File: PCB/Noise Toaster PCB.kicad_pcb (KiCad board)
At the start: 2 copper layers, 132.1 x 68.6 mm, 137 parts, among them J2 Power, J3 AREG, J4 LFO, J5 VCO, J6 VCO, J7 VCLPF, J8 VCA, J9 Amp, Q1 2N5457, Q10 2N3906, Q2 2N3904, Q3 2N3904, Q4 2N3904, Q5 2N3904, Q6 2N3904, Q7 2N5457, Q8 2N5457, Q9 2N5457, U1 LM324, U2 LM324, U3 LM386, X4 WNS

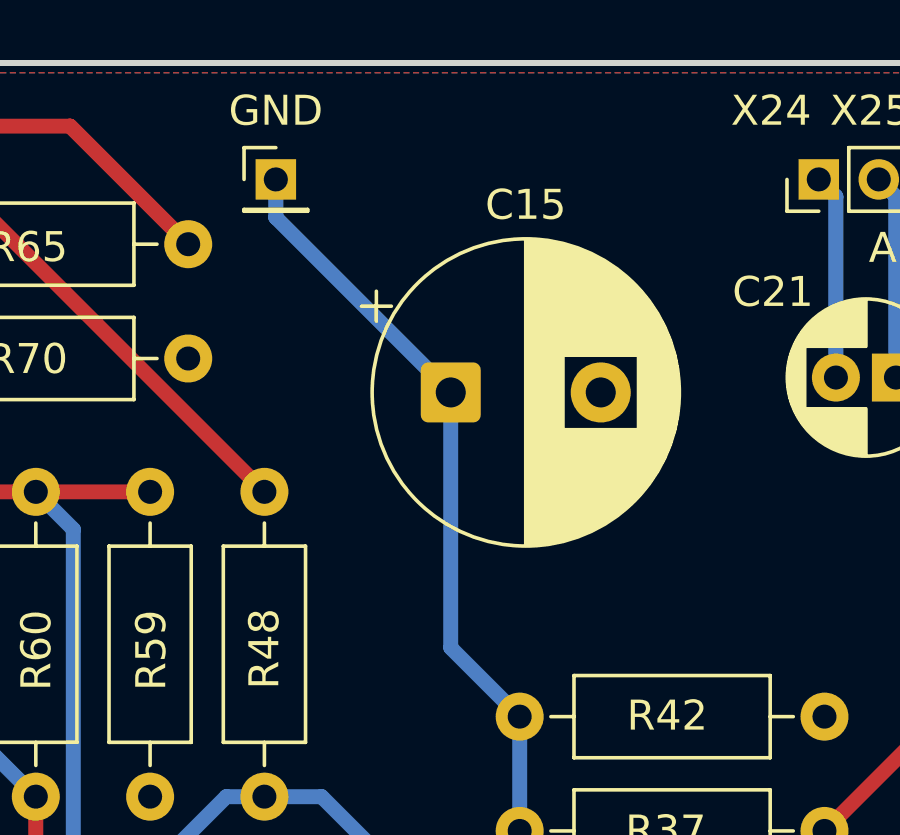
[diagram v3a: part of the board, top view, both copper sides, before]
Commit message: Added extra GND holes
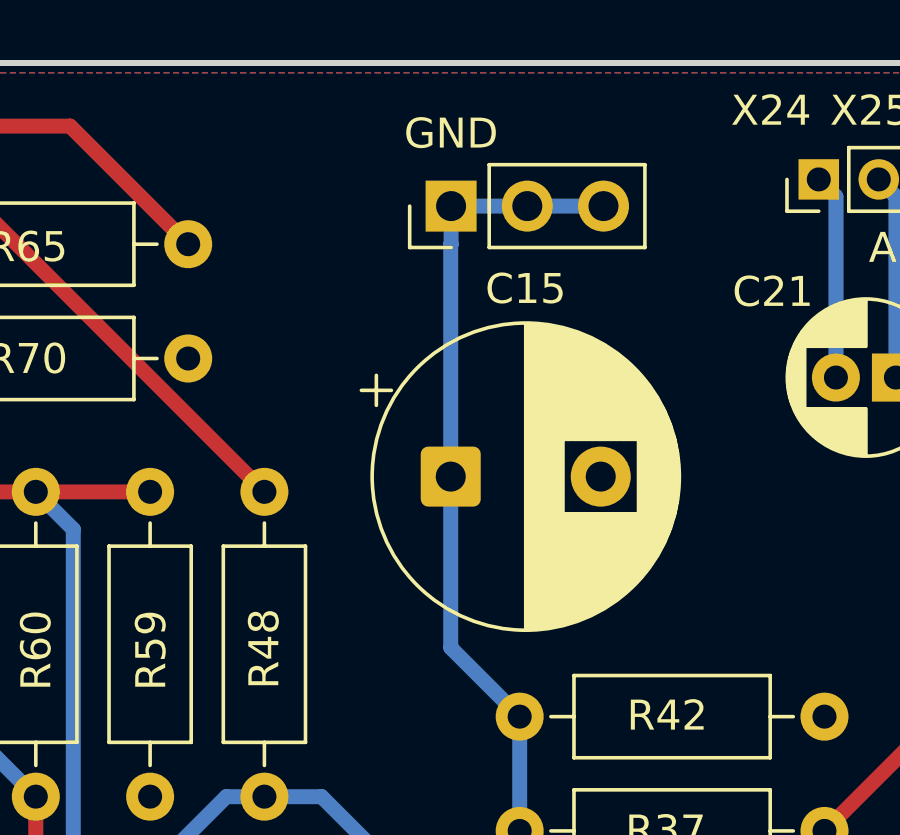
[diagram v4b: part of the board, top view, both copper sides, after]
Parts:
- GND: renamed from GND1; footprint Connector_PinHeader_2.00mm:PinHeader_1x01_P2.00mm_Vertical -> Connector_PinHeader_2.54mm:PinHeader_1x03_P2.54mm_Vertical
- moved GND 5.91 mm to (142.1, 80.0), turned to 90 degrees
- moved C15 2.81 mm to (142.1, 89.1)
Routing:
- net GND: track 160.9 -> 162.7 mm
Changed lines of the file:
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@@
 		)
 	)
-	(footprint "Connector_PinHeader_2.00mm:PinHeader_1x01_P2.00mm_Vertical"
+	(footprint "Connector_PinHeader_2.54mm:PinHeader_1x03_P2.54mm_Vertical"
 		(layer "F.Cu")
-		(at 136.302 79.148)
-		(descr "Through hole straight pin header, 1x01, 2.00mm pitch, single row")
-		(tags "Through hole pin header THT 1x01 2.00mm single row")
-		(property "Reference" "GND1"
-			(at 0 -2.06 0)
+		(at 142.144 80.037 90)
+		(descr "Through hole straight pin header, 1x03, 2.54mm pitch, single row")
+		(tags "Through hole pin header THT 1x03 2.54mm single row")
+		(property "Reference" "GND"
+			(at 2.413 0 180)
 			(layer "F.SilkS")
-			(hide yes)
 			(effects
 				(font
@@
 		)
 		(property "Value" "GND"
-			(at 0 -2.286 0)
-			(layer "F.SilkS")
+			(at 2.159 0 180)
+			(layer "F.Fab")
 			(effects
 				(font
@@
 		)
 		(property "Datasheet" ""
-			(at 0 0 0)
+			(at 0 0 90)
 			(layer "F.Fab")
 			(hide yes)
@@
 			)
 		)
-		(property "Description" "Generic connector, single row, 01x01, script generated"
-			(at 0 0 0)
+		(property "Description" ""
+			(at 0 0 90)
 			(layer "F.Fab")
 			(hide yes)
@@
 			)
 		)
+		(property "KiLib_Generator" "connector/pin_header_socket"
+			(at 0 0 90)
+			(layer "F.SilkS")
+			(hide yes)
+			(effects
+				(font
+					(size 1 1)
+					(thickness 0.15)
+				)
+			)
+		)
 		(sheetname "Power Supply")
 		(sheetfile "ps.kicad_sch")
@@
 		(duplicate_pad_numbers_are_jumpers no)
 		(fp_line
-			(start -1.06 -1.06)
-			(end 0 -1.06)
+			(start -1.38 -1.38)
+			(end 0 -1.38)
 			(stroke
 				(width 0.12)
@@
 		)
 		(fp_line
-			(start -1.06 0)
-			(end -1.06 -1.06)
+			(start -1.38 0)
+			(end -1.38 -1.38)
 			(stroke
 				(width 0.12)
@@
 		)
 		(fp_line
-			(start -1.06 1)
-			(end -1.06 1.06)
+			(start 1.38 1.27)
+			(end 1.38 6.46)
 			(stroke
 				(width 0.12)
@@
 		)
 		(fp_line
-			(start -1.06 1)
-			(end 1.06 1)
+			(start -1.38 1.27)
+			(end 1.38 1.27)
 			(stroke
 				(width 0.12)
@@
 		)
 		(fp_line
-			(start -1.06 1.06)
-			(end 1.06 1.06)
+			(start -1.38 1.27)
+			(end -1.38 6.46)
 			(stroke
 				(width 0.12)
@@
 		)
 		(fp_line
-			(start 1.06 1)
-			(end 1.06 1.06)
+			(start -1.38 6.46)
+			(end 1.38 6.46)
 			(stroke
 				(width 0.12)
@@
 			(layer "F.SilkS")
 		)
-		(fp_line
-			(start -1.5 -1.5)
-			(end -1.5 1.5)
-			(stroke
-				(width 0.05)
-				(type solid)
-			)
-			(layer "F.CrtYd")
-		)
-		(fp_line
-			(start -1.5 1.5)
-			(end 1.5 1.5)
-			(stroke
-				(width 0.05)
-				(type solid)
-			)
-			(layer "F.CrtYd")
-		)
-		(fp_line
-			(start 1.5 -1.5)
-			(end -1.5 -1.5)
+		(fp_rect
+			(start -1.77 -1.77)
+			(end 1.77 6.85)
 			(stroke
 				(width 0.05)
 				(type solid)
 			)
+			(fill no)
 			(layer "F.CrtYd")
 		)
 		(fp_line
-			(start 1.5 1.5)
-			(end 1.5 -1.5)
-			(stroke
-				(width 0.05)
-				(type solid)
-			)
-			(layer "F.CrtYd")
-		)
-		(fp_line
-			(start -1 -0.5)
-			(end -0.5 -1)
+			(start 1.27 -1.27)
+			(end 1.27 6.35)
 			(stroke
 				(width 0.1)
@@
 		)
 		(fp_line
-			(start -1 1)
-			(end -1 -0.5)
+			(start -0.635 -1.27)
+			(end 1.27 -1.27)
 			(stroke
 				(width 0.1)
@@
 		)
 		(fp_line
-			(start -0.5 -1)
-			(end 1 -1)
+			(start -1.27 -0.635)
+			(end -0.635 -1.27)
 			(stroke
 				(width 0.1)
@@
 		)
 		(fp_line
-			(start 1 -1)
-			(end 1 1)
+			(start 1.27 6.35)
+			(end -1.27 6.35)
 			(stroke
 				(width 0.1)
@@
 		)
 		(fp_line
-			(start 1 1)
-			(end -1 1)
+			(start -1.27 6.35)
+			(end -1.27 -0.635)
 			(stroke
 				(width 0.1)
@@
 			(layer "F.Fab")
 		)
+		(fp_text user "${REFERENCE}"
+			(at 0 2.54 0)
+			(layer "F.Fab")
+			(effects
+				(font
+					(size 1 1)
+					(thickness 0.15)
+				)
+			)
+		)
 		(pad "1" thru_hole rect
-			(at 0 0)
-			(size 1.35 1.35)
-			(drill 0.8)
+			(at 0 0 90)
+			(size 1.7 1.7)
+			(drill 1)
 			(layers "*.Cu" "*.Mask")
 			(remove_unused_layers no)
@@
 			(pintype "passive")
 		)
+		(pad "2" thru_hole circle
+			(at 0 2.54 90)
+			(size 1.7 1.7)
+			(drill 1)
+			(layers "*.Cu" "*.Mask")
+			(remove_unused_layers no)
+			(net "GND")
+		)
+		(pad "3" thru_hole circle
+			(at 0 5.08 90)
+			(size 1.7 1.7)
+			(drill 1)
+			(layers "*.Cu" "*.Mask")
+			(remove_unused_layers no)
+			(net "GND")
+		)
 		(embedded_fonts no)
-		(model "${KICAD6_3DMODEL_DIR}/Connector_PinHeader_2.00mm.3dshapes/PinHeader_1x01_P2.00mm_Vertical.wrl"
+		(model "${KICAD10_3DMODEL_DIR}/Connector_PinHeader_2.54mm.3dshapes/PinHeader_1x03_P2.54mm_Vertical.step"
 			(offset
 				(xyz 0 0 0)
@@
 	(footprint "Capacitor_THT:CP_Radial_D10.0mm_P5.00mm"
 		(layer "F.Cu")
-		(at 142.132272 86.248272)
+		(at 142.132272 89.054)
 		(descr "CP, Radial series, Radial, pin pitch=5.00mm, diameter=10mm, height=16mm, Electrolytic Capacitor")
 		(tags "CP Radial series Radial pin pitch 5.00mm diameter 10mm height 16mm Electrolytic Capacitor")
@@
 	)
 	(segment
-		(start 121.189 100.357)
-		(end 125.106 104.274)
+		(start 144.684 80.037)
+		(end 142.144 80.037)
 		(width 0.5)
 		(layer "B.Cu")
@@
 	)
 	(segment
-		(start 136.302 80.418)
-		(end 142.132272 86.248272)
+		(start 121.189 100.357)
+		(end 125.106 104.274)
 		(width 0.5)
 		(layer "B.Cu")
@@
 	)
 	(segment
+		(start 147.224 80.037)
+		(end 144.684 80.037)
+		(width 0.5)
+		(layer "B.Cu")
+		(net "GND")
+	)
+	(segment
 		(start 148.621 120.042)
 		(end 148.621 134.679)
@@
 	)
 	(segment
-		(start 137.826 126.752)
-		(end 137.826 124.36)
+		(start 142.144 81.307)
+		(end 142.132272 81.318728)
 		(width 0.5)
 		(layer "B.Cu")
@@
 	)
 	(segment
-		(start 142.132272 86.248272)
-		(end 142.132272 94.757272)
-		(width 0.5)
-		(layer "B.Cu")
-		(net "GND")
-	)
-	(segment
-		(start 136.302 79.148)
-		(end 136.302 80.418)
+		(start 137.826 126.752)
+		(end 137.826 124.36)
 		(width 0.5)
 		(layer "B.Cu")
@@
 		(width 0.5)
 		(layer "B.Cu")
+		(net "GND")
+	)
+	(segment
+		(start 142.144 80.037)
+		(end 142.144 81.307)
+		(width 0.5)
+		(layer "B.Cu")
+		(net "GND")
+	)
+	(segment
+		(start 142.132272 81.318728)
+		(end 142.132272 94.757272)
+		(width 0.5)
+		(layer "B.Cu")

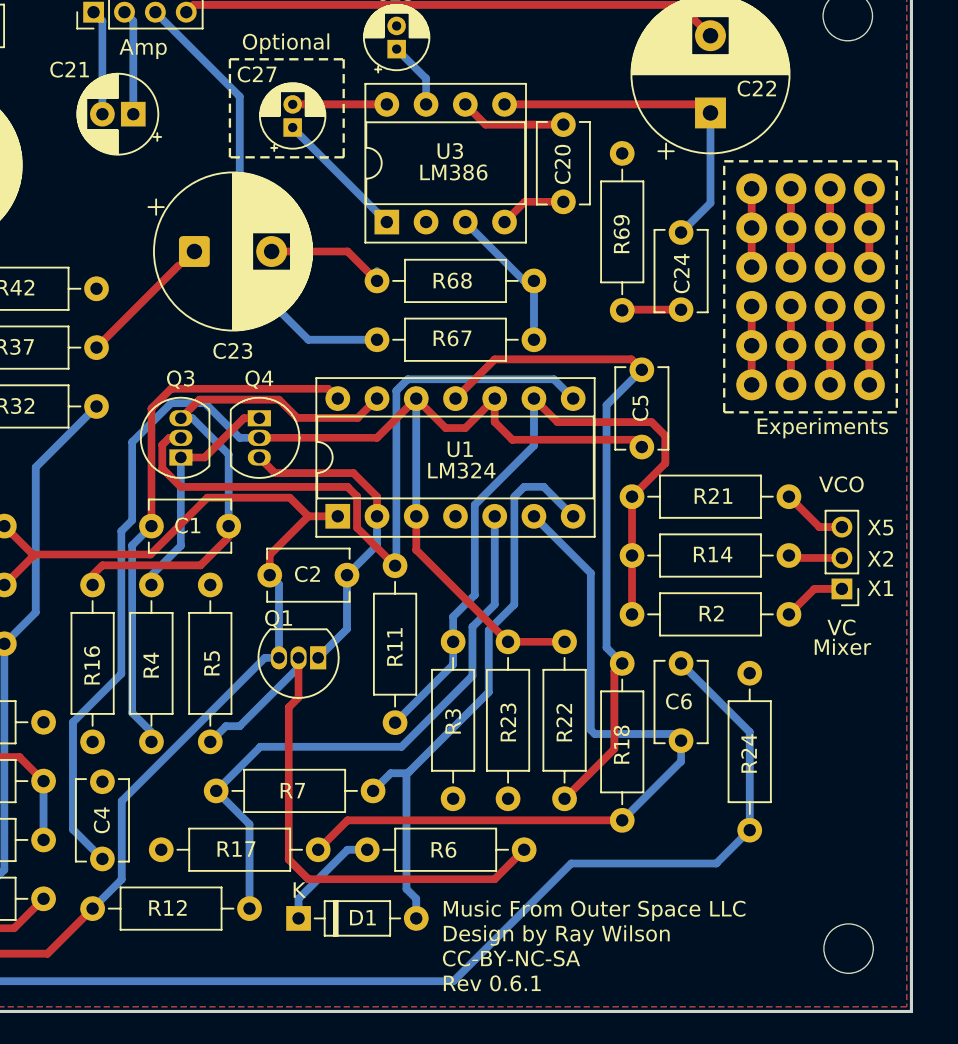
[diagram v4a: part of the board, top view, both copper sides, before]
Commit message: Re added VCO CV Mod pad
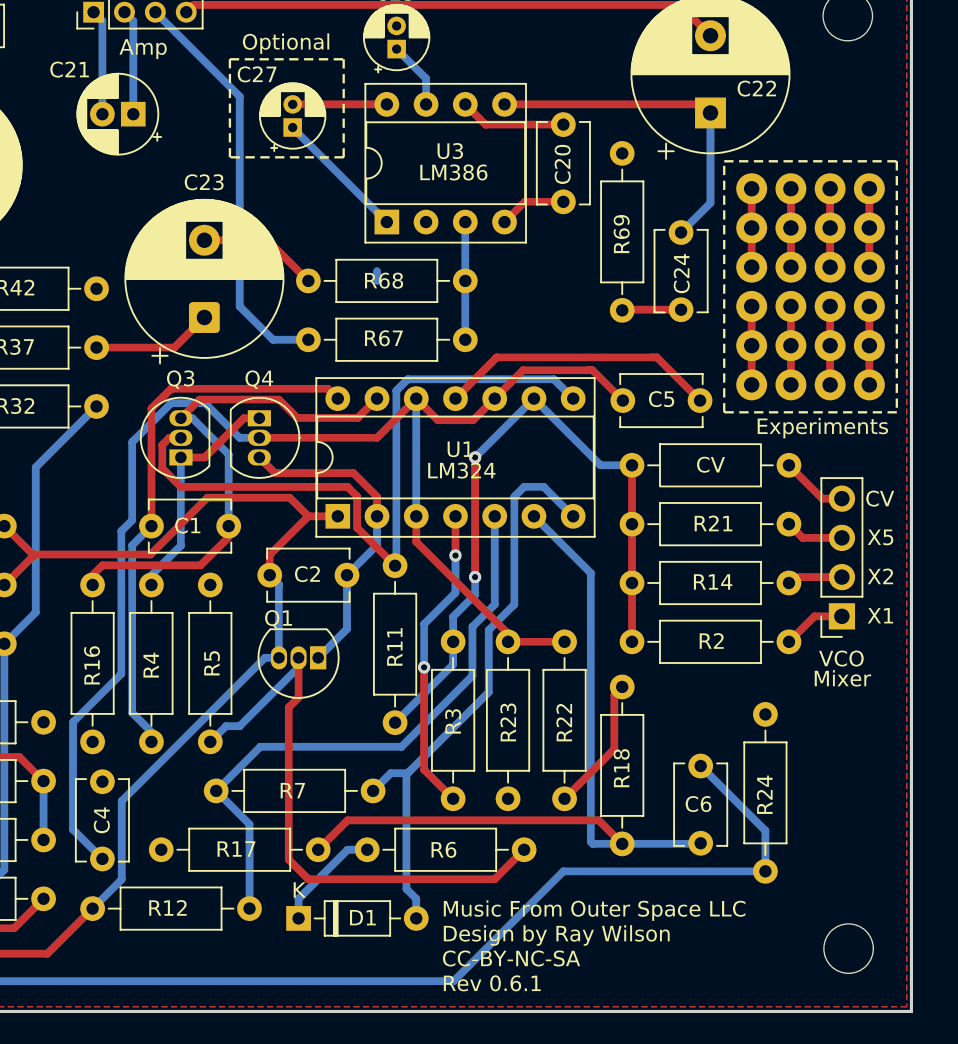
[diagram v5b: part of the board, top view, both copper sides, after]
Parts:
- added CV: R_Axial_DIN0207_L6.3mm_D2.5mm_P10.16mm_Horizontal, Resistor_THT:R_Axial_DIN0207_L6.3mm_D2.5mm_P10.16mm_Horizontal, F.Cu at (189.3, 108.5)
- VCO: renamed from J5; footprint Connector_PinHeader_2.00mm:PinHeader_1x03_P2.00mm_Vertical -> Connector_PinSocket_2.54mm:PinSocket_1x04_P2.54mm_Vertical
- moved C6 6.76 mm to (193.7, 128.0)
- moved R67 4.44 mm to (178.5, 100.4)
- moved R68 4.44 mm to (178.5, 96.5)
- moved C23 4.32 mm to (161.6, 98.9), turned to 90 degrees
- moved C5 3.25 mm to (188.7, 104.3), turned to 0 degrees
- moved R24 2.85 mm to (197.9, 134.8)
- moved R14 1.78 mm to (189.3, 116.1)
- moved R2 1.78 mm to (189.3, 119.9)
- moved R21 1.78 mm to (189.3, 112.3)
- moved VCO 1.78 mm to (202.8, 118.3)
- moved R18 1.52 mm to (188.6, 133.0)
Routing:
- net B+: track 38.5 -> 58.7 mm, vias 0 -> 2
- net B-: track 128.7 -> 111.7 mm
- net (no net): track 40.6 -> 45.0 mm
- net /Front Panel/X6: track 69.1 -> 64.9 mm
- net /Audio Amplifier/X27: track 29.8 -> 26.7 mm
- net Net-(U1C--): track 46.7 -> 44.3 mm, vias 0 -> 2
- net /G2: track 91.0 -> 88.8 mm
- net Net-(U3-+): track 9.83 -> 7.62 mm
- net Net-(U1B--): track 48.7 -> 50.9 mm

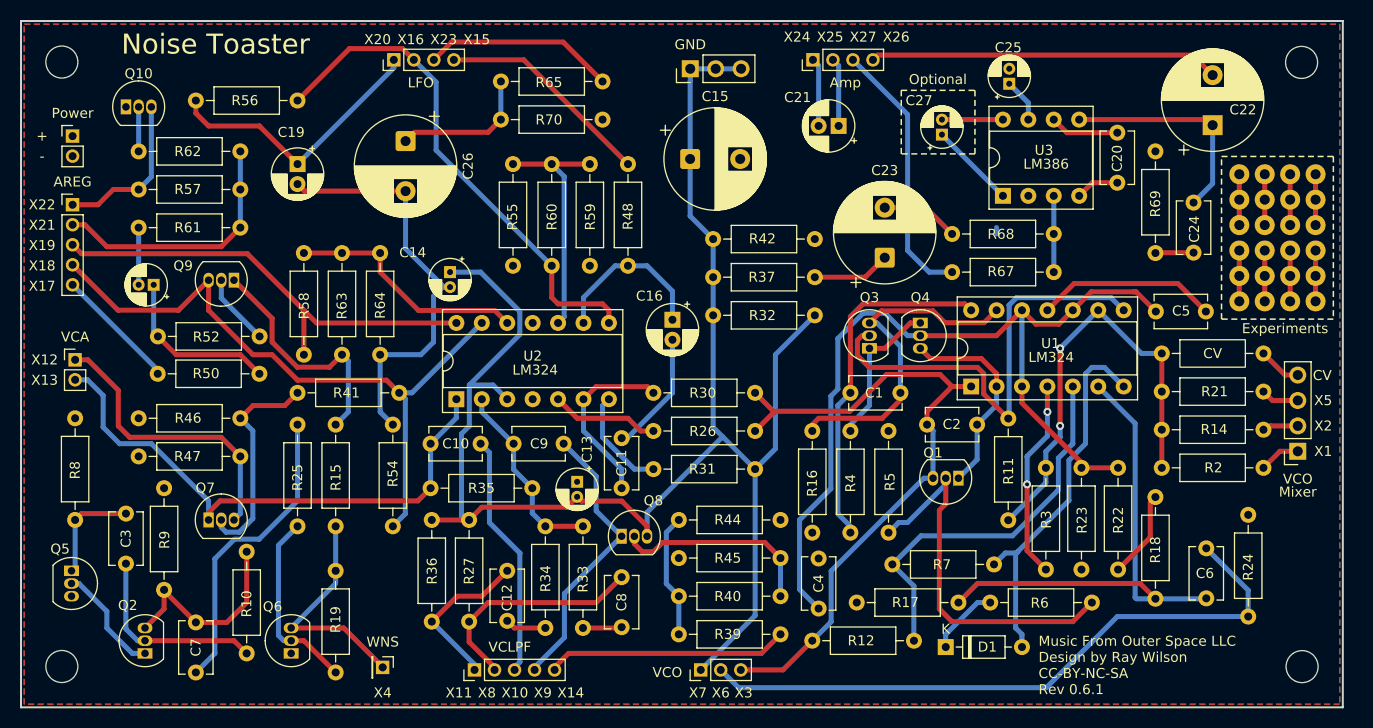
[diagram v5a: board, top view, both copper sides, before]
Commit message: Change Headers to 2.54mm
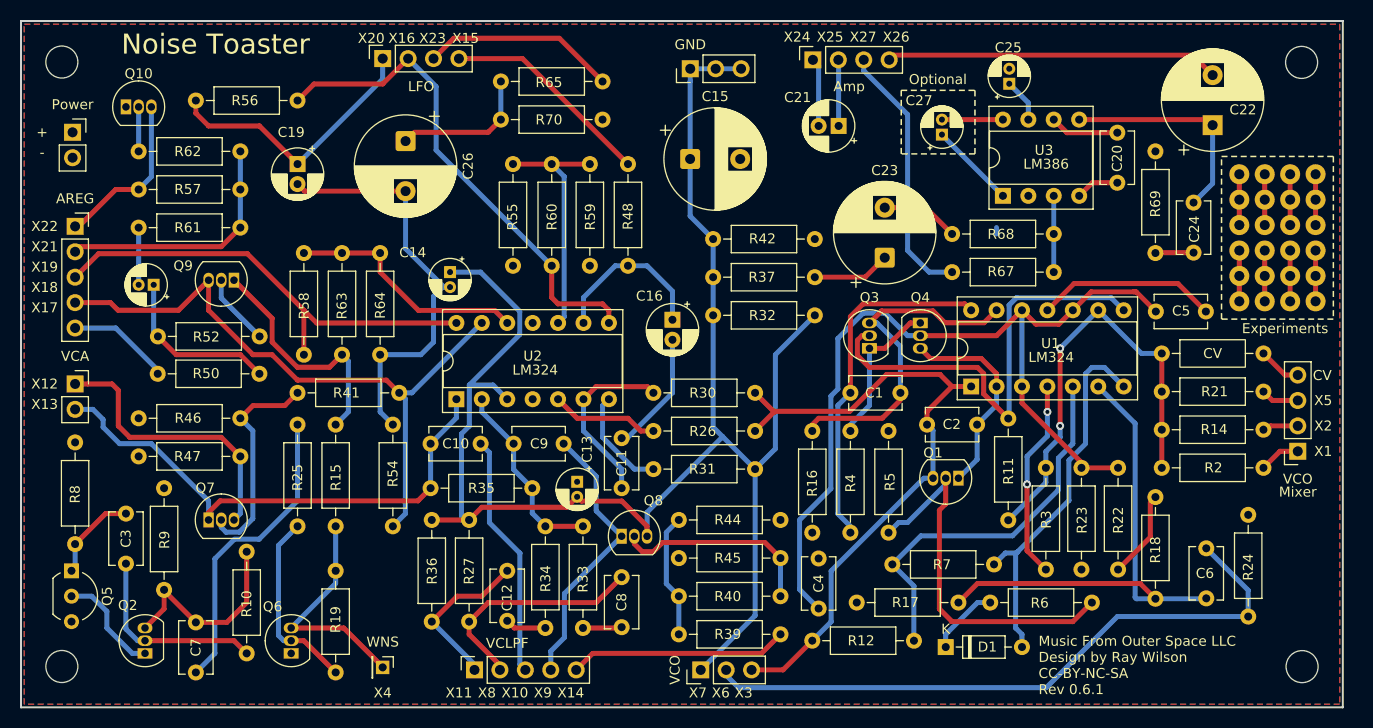
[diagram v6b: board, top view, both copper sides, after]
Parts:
- AREG: renamed from J3; footprint Connector_PinHeader_2.00mm:PinHeader_1x05_P2.00mm_Vertical -> Connector_PinSocket_2.54mm:PinSocket_1x05_P2.54mm_Vertical
- Amp: renamed from J9; footprint Connector_PinHeader_2.00mm:PinHeader_1x04_P2.00mm_Vertical -> Connector_PinSocket_2.54mm:PinSocket_1x04_P2.54mm_Vertical
- LFO: renamed from J4; footprint Connector_PinHeader_2.00mm:PinHeader_1x04_P2.00mm_Vertical -> Connector_PinSocket_2.54mm:PinSocket_1x04_P2.54mm_Vertical
- Power: renamed from J2; footprint Connector_PinHeader_2.00mm:PinHeader_1x02_P2.00mm_Vertical -> Connector_PinSocket_2.54mm:PinSocket_1x02_P2.54mm_Vertical
- Q5: footprint Package_TO_SOT_THT:TO-92_Inline -> Package_TO_SOT_THT:TO-92_Inline_Wide
- VCA: renamed from J8; footprint Connector_PinHeader_2.00mm:PinHeader_1x02_P2.00mm_Vertical -> Connector_PinSocket_2.54mm:PinSocket_1x02_P2.54mm_Vertical
- VCLPF: renamed from J7; footprint Connector_PinHeader_2.00mm:PinHeader_1x05_P2.00mm_Vertical -> Connector_PinSocket_2.54mm:PinSocket_1x05_P2.54mm_Vertical
- VCO: renamed from J6; footprint Connector_PinHeader_2.00mm:PinHeader_1x03_P2.00mm_Vertical -> Connector_PinHeader_2.54mm:PinHeader_1x03_P2.54mm_Vertical
- moved R8 2.41 mm to (80.7, 117.4)
- moved VCA 2.41 mm to (80.7, 111.5)
- moved AREG 2.17 mm to (80.7, 95.8)
- moved LFO 1.12 mm to (111.4, 79.0)
- moved Power 0.38 mm to (80.4, 86.4)
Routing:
- net /FO: track 56.0 -> 53.4 mm
- net /Front Panel/X14: track 23.9 -> 21.9 mm
- net /Attack Release Envelope Generator/X17: track 12.0 -> 9.99 mm
- net /ARG: track 67.4 -> 65.6 mm
- net /Audio Amplifier/X26: track 35.0 -> 33.3 mm
- net Net-(Q5-E): track 10.6 -> 9.16 mm
- net /Front Panel/B: track 51.2 -> 50.1 mm
- net /RMP: track 67.7 -> 66.6 mm
- net /Front Panel/X12: track 29.2 -> 28.2 mm
- net /Attack Release Envelope Generator/X21: track 26.1 -> 25.1 mm
- net /Attack Release Envelope Generator/X22: track 16.0 -> 16.7 mm
- net B-: track 111.7 -> 111.2 mm
